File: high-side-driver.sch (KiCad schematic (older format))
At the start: 10 parts, among them Q1 CJ3139K, Q2 CJ3139K, Q3 CJ3139K, Q4 CJ3139K, Q5 CJ3139K, Q6 CJ3139K, Q7 CJ3139K, Q8 CJ3139K, U8 74HC595

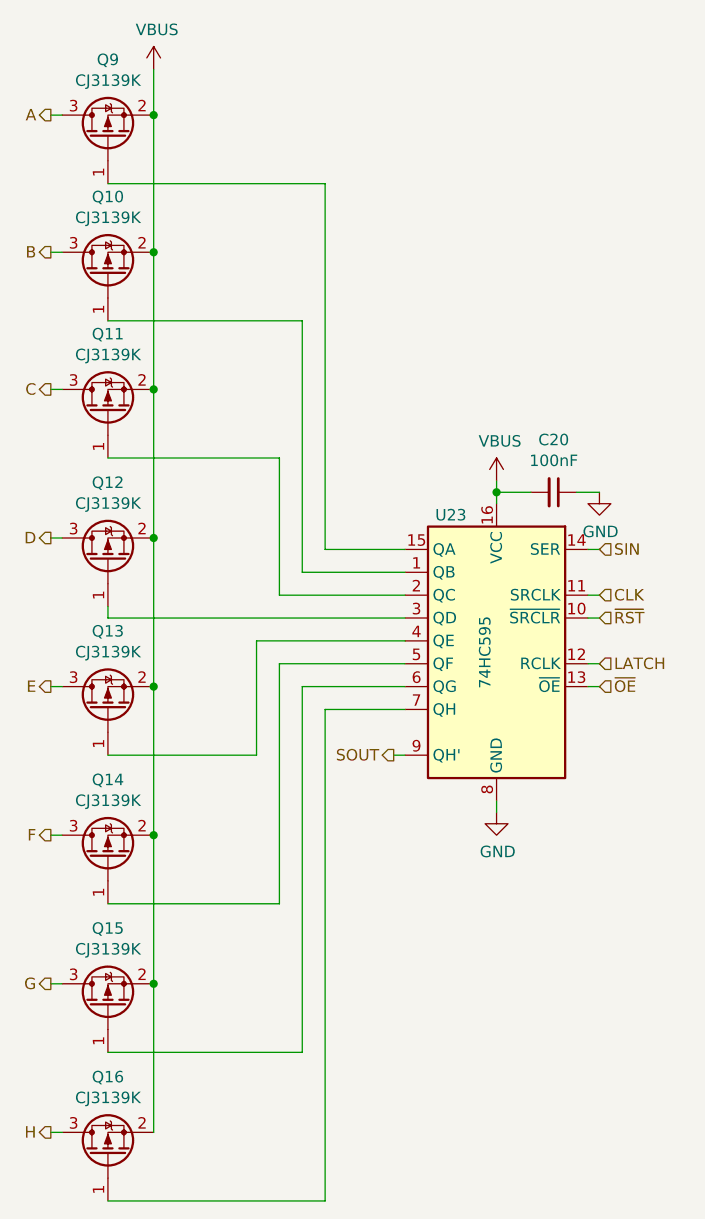
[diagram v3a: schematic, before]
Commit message: Add multiplexing MCU and USB
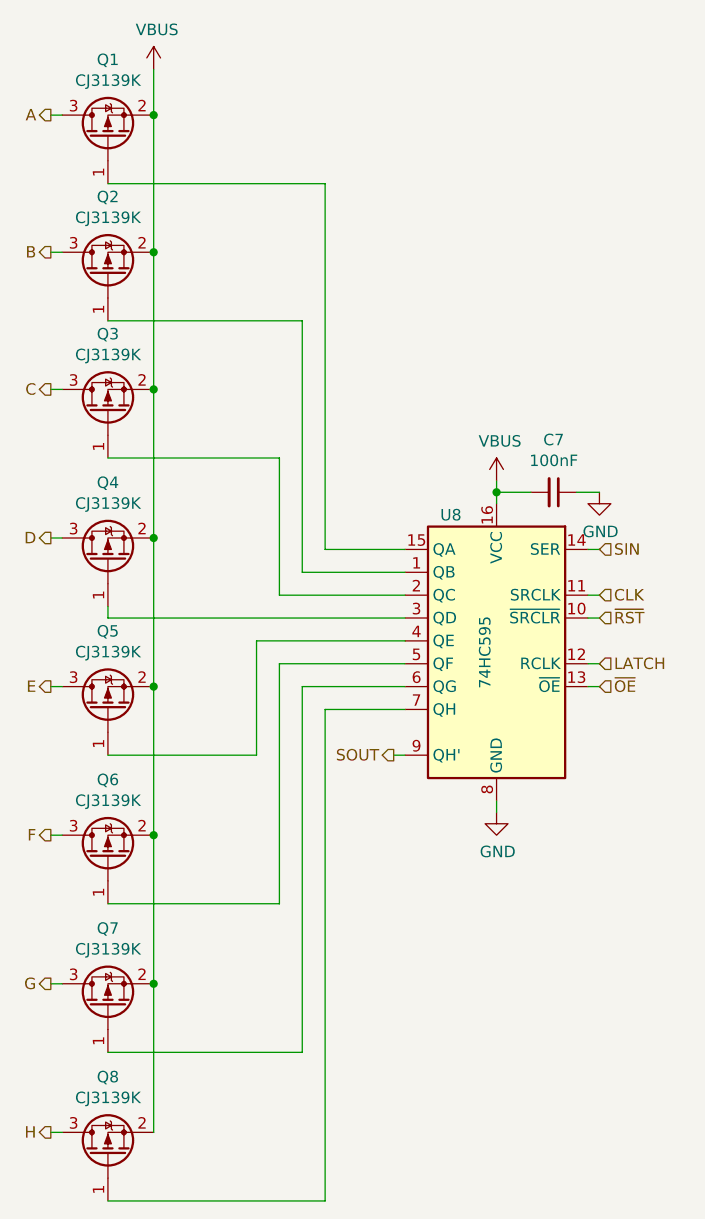
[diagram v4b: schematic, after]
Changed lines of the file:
@@
 $Descr A4 11693 8268
 encoding utf-8
-Sheet 24 25
+Sheet 9 25
 Title ""
 Date ""
@@
 AR Path="/61C25DCC/61C27AAF" Ref="#PWR0119"  Part="1"
 AR Path="/61C56D3D/61C27AAF" Ref="#PWR0159"  Part="1"
-F 0 "#PWR0159" H 5500 4100 50  0001 C CNN
+F 0 "#PWR0119" H 5500 4100 50  0001 C CNN
 F 1 "GND" H 5505 4177 50  0000 C CNN
 F 2 "" H 5500 4350 50  0001 C CNN
@@
 AR Path="/61C25DCC/61C27AC2" Ref="#PWR0120"  Part="1"
 AR Path="/61C56D3D/61C27AC2" Ref="#PWR0160"  Part="1"
-F 0 "#PWR0160" H 5950 2700 50  0001 C CNN
+F 0 "#PWR0120" H 5950 2700 50  0001 C CNN
 F 1 "GND" H 5955 2777 50  0000 C CNN
 F 2 "" H 5950 2950 50  0001 C CNN
@@
 AR Path="/61C25DCC/61C27AC9" Ref="C7"  Part="1"
 AR Path="/61C56D3D/61C27AC9" Ref="C20"  Part="1"
-F 0 "C20" V 5521 2950 50  0000 C CNN
+F 0 "C7" V 5521 2950 50  0000 C CNN
 F 1 "100nF" V 5612 2950 50  0000 C CNN
 F 2 "Capacitor_SMD:C_0402_1005Metric" H 5750 2950 50  0001 C CNN
@@
 AR Path="/61C25DCC/61C27AE4" Ref="#PWR0121"  Part="1"
 AR Path="/61C56D3D/61C27AE4" Ref="#PWR0161"  Part="1"
-F 0 "#PWR0161" H 5500 2750 50  0001 C CNN
+F 0 "#PWR0121" H 5500 2750 50  0001 C CNN
 F 1 "VBUS" H 5515 3073 50  0000 C CNN
 F 2 "" H 5500 2900 50  0001 C CNN
@@
 AR Path="/61C25DCC/61C27AFF" Ref="U8"  Part="1"
 AR Path="/61C56D3D/61C27AFF" Ref="U23"  Part="1"
-F 0 "U23" H 5700 4150 50  0000 C CNN
+F 0 "U8" H 5700 4150 50  0000 C CNN
 F 1 "74HC595" V 5550 3550 50  0000 C CNN
 F 2 "Package_Texas:X1QFN-16-2.5x2.5-EP-1.2" H 5500 3600 50  0001 C CNN
@@
 AR Path="/61C25DCC/61C2F27B" Ref="Q1"  Part="1"
 AR Path="/61C56D3D/61C2F27B" Ref="Q9"  Part="1"
-F 0 "Q9" V 4142 1400 50  0000 C CNN
+F 0 "Q1" V 4142 1400 50  0000 C CNN
 F 1 "CJ3139K" V 4051 1400 50  0000 C CNN
 F 2 "Package_TO_SOT_SMD:SOT-723" H 4000 1325 50  0001 L CIN
@@
 AR Path="/61C25DCC/61C3FEA0" Ref="#PWR0122"  Part="1"
 AR Path="/61C56D3D/61C3FEA0" Ref="#PWR0162"  Part="1"
-F 0 "#PWR0162" H 4000 950 50  0001 C CNN
+F 0 "#PWR0122" H 4000 950 50  0001 C CNN
 F 1 "VBUS" H 4015 1273 50  0000 C CNN
 F 2 "" H 4000 1100 50  0001 C CNN
@@
 AR Path="/61C25DCC/61C8820B" Ref="Q2"  Part="1"
 AR Path="/61C56D3D/61C8820B" Ref="Q10"  Part="1"
-F 0 "Q10" V 4142 2000 50  0000 C CNN
+F 0 "Q2" V 4142 2000 50  0000 C CNN
 F 1 "CJ3139K" V 4051 2000 50  0000 C CNN
 F 2 "Package_TO_SOT_SMD:SOT-723" H 4000 1925 50  0001 L CIN
@@
 AR Path="/61C25DCC/61C89C26" Ref="Q3"  Part="1"
 AR Path="/61C56D3D/61C89C26" Ref="Q11"  Part="1"
-F 0 "Q11" V 4142 2600 50  0000 C CNN
+F 0 "Q3" V 4142 2600 50  0000 C CNN
 F 1 "CJ3139K" V 4051 2600 50  0000 C CNN
 F 2 "Package_TO_SOT_SMD:SOT-723" H 4000 2525 50  0001 L CIN
@@
 AR Path="/61C25DCC/61C8B69B" Ref="Q4"  Part="1"
 AR Path="/61C56D3D/61C8B69B" Ref="Q12"  Part="1"
-F 0 "Q12" V 4142 3250 50  0000 C CNN
+F 0 "Q4" V 4142 3250 50  0000 C CNN
 F 1 "CJ3139K" V 4051 3250 50  0000 C CNN
 F 2 "Package_TO_SOT_SMD:SOT-723" H 4000 3175 50  0001 L CIN
@@
 AR Path="/61C25DCC/61C8D443" Ref="Q5"  Part="1"
 AR Path="/61C56D3D/61C8D443" Ref="Q13"  Part="1"
-F 0 "Q13" V 4142 3900 50  0000 C CNN
+F 0 "Q5" V 4142 3900 50  0000 C CNN
 F 1 "CJ3139K" V 4051 3900 50  0000 C CNN
 F 2 "Package_TO_SOT_SMD:SOT-723" H 4000 3825 50  0001 L CIN
@@
 AR Path="/61C25DCC/61C8EABF" Ref="Q6"  Part="1"
 AR Path="/61C56D3D/61C8EABF" Ref="Q14"  Part="1"
-F 0 "Q14" V 4142 4550 50  0000 C CNN
+F 0 "Q6" V 4142 4550 50  0000 C CNN
 F 1 "CJ3139K" V 4051 4550 50  0000 C CNN
 F 2 "Package_TO_SOT_SMD:SOT-723" H 4000 4475 50  0001 L CIN
@@
 AR Path="/61C25DCC/61C901AA" Ref="Q7"  Part="1"
 AR Path="/61C56D3D/61C901AA" Ref="Q15"  Part="1"
-F 0 "Q15" V 4142 5200 50  0000 C CNN
+F 0 "Q7" V 4142 5200 50  0000 C CNN
 F 1 "CJ3139K" V 4051 5200 50  0000 C CNN
 F 2 "Package_TO_SOT_SMD:SOT-723" H 4000 5125 50  0001 L CIN
@@
 AR Path="/61C25DCC/61C923B7" Ref="Q8"  Part="1"
 AR Path="/61C56D3D/61C923B7" Ref="Q16"  Part="1"
-F 0 "Q16" V 4142 5850 50  0000 C CNN
+F 0 "Q8" V 4142 5850 50  0000 C CNN
 F 1 "CJ3139K" V 4051 5850 50  0000 C CNN
 F 2 "Package_TO_SOT_SMD:SOT-723" H 4000 5775 50  0001 L CIN

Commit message: Add mounting pad for safety pin
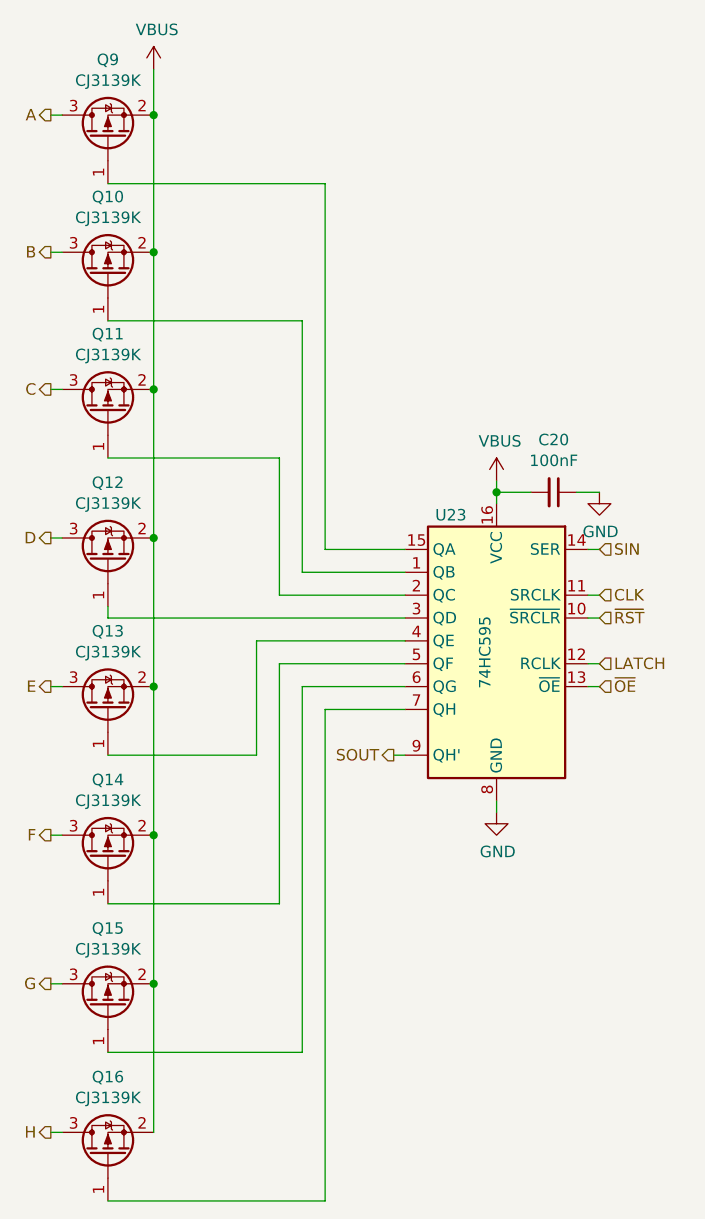
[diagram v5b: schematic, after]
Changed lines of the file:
@@
 AR Path="/61C25DCC/61C27AAF" Ref="#PWR0119"  Part="1"
 AR Path="/61C56D3D/61C27AAF" Ref="#PWR0159"  Part="1"
-F 0 "#PWR0119" H 5500 4100 50  0001 C CNN
+F 0 "#PWR0159" H 5500 4100 50  0001 C CNN
 F 1 "GND" H 5505 4177 50  0000 C CNN
 F 2 "" H 5500 4350 50  0001 C CNN
@@
 AR Path="/61C25DCC/61C27AC2" Ref="#PWR0120"  Part="1"
 AR Path="/61C56D3D/61C27AC2" Ref="#PWR0160"  Part="1"
-F 0 "#PWR0120" H 5950 2700 50  0001 C CNN
+F 0 "#PWR0160" H 5950 2700 50  0001 C CNN
 F 1 "GND" H 5955 2777 50  0000 C CNN
 F 2 "" H 5950 2950 50  0001 C CNN
@@
 AR Path="/61C25DCC/61C27AC9" Ref="C7"  Part="1"
 AR Path="/61C56D3D/61C27AC9" Ref="C20"  Part="1"
-F 0 "C7" V 5521 2950 50  0000 C CNN
+F 0 "C20" V 5521 2950 50  0000 C CNN
 F 1 "100nF" V 5612 2950 50  0000 C CNN
 F 2 "Capacitor_SMD:C_0402_1005Metric" H 5750 2950 50  0001 C CNN
@@
 AR Path="/61C25DCC/61C27AE4" Ref="#PWR0121"  Part="1"
 AR Path="/61C56D3D/61C27AE4" Ref="#PWR0161"  Part="1"
-F 0 "#PWR0121" H 5500 2750 50  0001 C CNN
+F 0 "#PWR0161" H 5500 2750 50  0001 C CNN
 F 1 "VBUS" H 5515 3073 50  0000 C CNN
 F 2 "" H 5500 2900 50  0001 C CNN
@@
 AR Path="/61C25DCC/61C27AFF" Ref="U8"  Part="1"
 AR Path="/61C56D3D/61C27AFF" Ref="U23"  Part="1"
-F 0 "U8" H 5700 4150 50  0000 C CNN
+F 0 "U23" H 5700 4150 50  0000 C CNN
 F 1 "74HC595" V 5550 3550 50  0000 C CNN
 F 2 "Package_Texas:X1QFN-16-2.5x2.5-EP-1.2" H 5500 3600 50  0001 C CNN
@@
 AR Path="/61C25DCC/61C2F27B" Ref="Q1"  Part="1"
 AR Path="/61C56D3D/61C2F27B" Ref="Q9"  Part="1"
-F 0 "Q1" V 4142 1400 50  0000 C CNN
+F 0 "Q9" V 4142 1400 50  0000 C CNN
 F 1 "CJ3139K" V 4051 1400 50  0000 C CNN
 F 2 "Package_TO_SOT_SMD:SOT-723" H 4000 1325 50  0001 L CIN
@@
 AR Path="/61C25DCC/61C3FEA0" Ref="#PWR0122"  Part="1"
 AR Path="/61C56D3D/61C3FEA0" Ref="#PWR0162"  Part="1"
-F 0 "#PWR0122" H 4000 950 50  0001 C CNN
+F 0 "#PWR0162" H 4000 950 50  0001 C CNN
 F 1 "VBUS" H 4015 1273 50  0000 C CNN
 F 2 "" H 4000 1100 50  0001 C CNN
@@
 AR Path="/61C25DCC/61C8820B" Ref="Q2"  Part="1"
 AR Path="/61C56D3D/61C8820B" Ref="Q10"  Part="1"
-F 0 "Q2" V 4142 2000 50  0000 C CNN
+F 0 "Q10" V 4142 2000 50  0000 C CNN
 F 1 "CJ3139K" V 4051 2000 50  0000 C CNN
 F 2 "Package_TO_SOT_SMD:SOT-723" H 4000 1925 50  0001 L CIN
@@
 AR Path="/61C25DCC/61C89C26" Ref="Q3"  Part="1"
 AR Path="/61C56D3D/61C89C26" Ref="Q11"  Part="1"
-F 0 "Q3" V 4142 2600 50  0000 C CNN
+F 0 "Q11" V 4142 2600 50  0000 C CNN
 F 1 "CJ3139K" V 4051 2600 50  0000 C CNN
 F 2 "Package_TO_SOT_SMD:SOT-723" H 4000 2525 50  0001 L CIN
@@
 AR Path="/61C25DCC/61C8B69B" Ref="Q4"  Part="1"
 AR Path="/61C56D3D/61C8B69B" Ref="Q12"  Part="1"
-F 0 "Q4" V 4142 3250 50  0000 C CNN
+F 0 "Q12" V 4142 3250 50  0000 C CNN
 F 1 "CJ3139K" V 4051 3250 50  0000 C CNN
 F 2 "Package_TO_SOT_SMD:SOT-723" H 4000 3175 50  0001 L CIN
@@
 AR Path="/61C25DCC/61C8D443" Ref="Q5"  Part="1"
 AR Path="/61C56D3D/61C8D443" Ref="Q13"  Part="1"
-F 0 "Q5" V 4142 3900 50  0000 C CNN
+F 0 "Q13" V 4142 3900 50  0000 C CNN
 F 1 "CJ3139K" V 4051 3900 50  0000 C CNN
 F 2 "Package_TO_SOT_SMD:SOT-723" H 4000 3825 50  0001 L CIN
@@
 AR Path="/61C25DCC/61C8EABF" Ref="Q6"  Part="1"
 AR Path="/61C56D3D/61C8EABF" Ref="Q14"  Part="1"
-F 0 "Q6" V 4142 4550 50  0000 C CNN
+F 0 "Q14" V 4142 4550 50  0000 C CNN
 F 1 "CJ3139K" V 4051 4550 50  0000 C CNN
 F 2 "Package_TO_SOT_SMD:SOT-723" H 4000 4475 50  0001 L CIN
@@
 AR Path="/61C25DCC/61C901AA" Ref="Q7"  Part="1"
 AR Path="/61C56D3D/61C901AA" Ref="Q15"  Part="1"
-F 0 "Q7" V 4142 5200 50  0000 C CNN
+F 0 "Q15" V 4142 5200 50  0000 C CNN
 F 1 "CJ3139K" V 4051 5200 50  0000 C CNN
 F 2 "Package_TO_SOT_SMD:SOT-723" H 4000 5125 50  0001 L CIN
@@
 AR Path="/61C25DCC/61C923B7" Ref="Q8"  Part="1"
 AR Path="/61C56D3D/61C923B7" Ref="Q16"  Part="1"
-F 0 "Q8" V 4142 5850 50  0000 C CNN
+F 0 "Q16" V 4142 5850 50  0000 C CNN
 F 1 "CJ3139K" V 4051 5850 50  0000 C CNN
 F 2 "Package_TO_SOT_SMD:SOT-723" H 4000 5775 50  0001 L CIN

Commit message: Use better ESP32 Pico D4 footprint
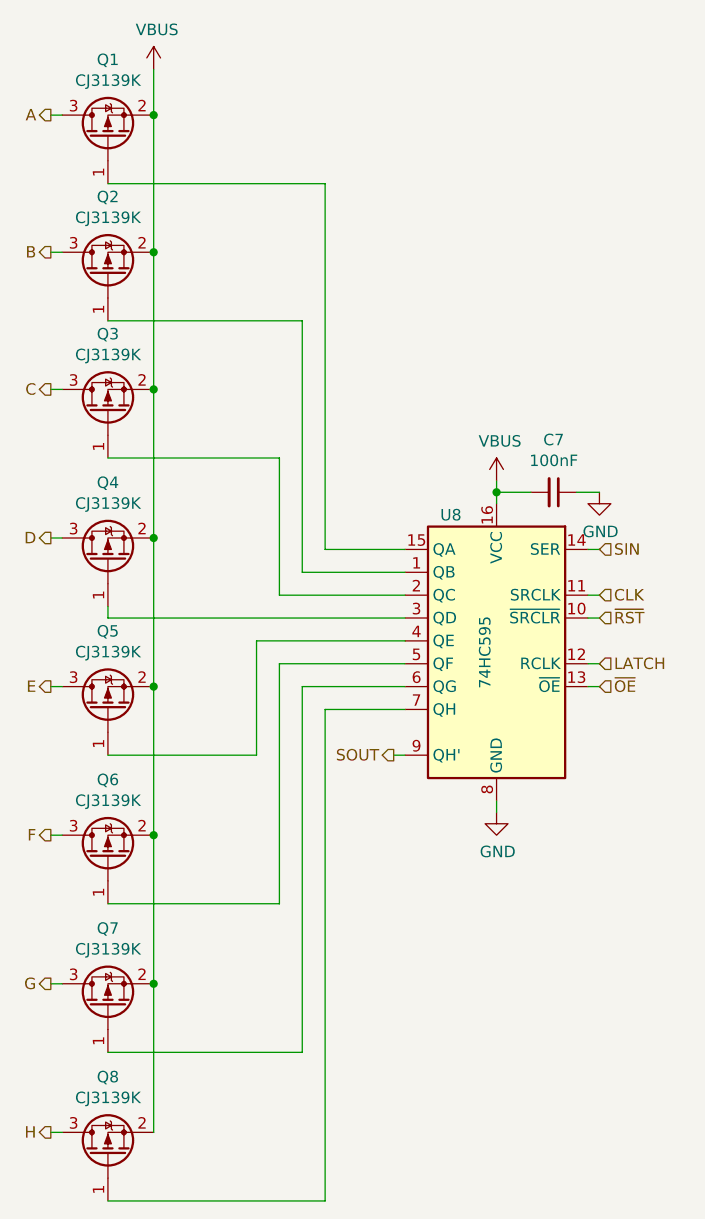
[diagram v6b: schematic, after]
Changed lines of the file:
@@
 AR Path="/61C25DCC/61C27AC9" Ref="C7"  Part="1"
 AR Path="/61C56D3D/61C27AC9" Ref="C20"  Part="1"
-F 0 "C20" V 5521 2950 50  0000 C CNN
+F 0 "C7" V 5521 2950 50  0000 C CNN
 F 1 "100nF" V 5612 2950 50  0000 C CNN
 F 2 "Capacitor_SMD:C_0402_1005Metric" H 5750 2950 50  0001 C CNN
@@
 AR Path="/61C25DCC/61C27AFF" Ref="U8"  Part="1"
 AR Path="/61C56D3D/61C27AFF" Ref="U23"  Part="1"
-F 0 "U23" H 5700 4150 50  0000 C CNN
+F 0 "U8" H 5700 4150 50  0000 C CNN
 F 1 "74HC595" V 5550 3550 50  0000 C CNN
 F 2 "Package_Texas:X1QFN-16-2.5x2.5-EP-1.2" H 5500 3600 50  0001 C CNN
@@
 AR Path="/61C25DCC/61C2F27B" Ref="Q1"  Part="1"
 AR Path="/61C56D3D/61C2F27B" Ref="Q9"  Part="1"
-F 0 "Q9" V 4142 1400 50  0000 C CNN
+F 0 "Q1" V 4142 1400 50  0000 C CNN
 F 1 "CJ3139K" V 4051 1400 50  0000 C CNN
 F 2 "Package_TO_SOT_SMD:SOT-723" H 4000 1325 50  0001 L CIN
@@
 AR Path="/61C25DCC/61C8820B" Ref="Q2"  Part="1"
 AR Path="/61C56D3D/61C8820B" Ref="Q10"  Part="1"
-F 0 "Q10" V 4142 2000 50  0000 C CNN
+F 0 "Q2" V 4142 2000 50  0000 C CNN
 F 1 "CJ3139K" V 4051 2000 50  0000 C CNN
 F 2 "Package_TO_SOT_SMD:SOT-723" H 4000 1925 50  0001 L CIN
@@
 AR Path="/61C25DCC/61C89C26" Ref="Q3"  Part="1"
 AR Path="/61C56D3D/61C89C26" Ref="Q11"  Part="1"
-F 0 "Q11" V 4142 2600 50  0000 C CNN
+F 0 "Q3" V 4142 2600 50  0000 C CNN
 F 1 "CJ3139K" V 4051 2600 50  0000 C CNN
 F 2 "Package_TO_SOT_SMD:SOT-723" H 4000 2525 50  0001 L CIN
@@
 AR Path="/61C25DCC/61C8B69B" Ref="Q4"  Part="1"
 AR Path="/61C56D3D/61C8B69B" Ref="Q12"  Part="1"
-F 0 "Q12" V 4142 3250 50  0000 C CNN
+F 0 "Q4" V 4142 3250 50  0000 C CNN
 F 1 "CJ3139K" V 4051 3250 50  0000 C CNN
 F 2 "Package_TO_SOT_SMD:SOT-723" H 4000 3175 50  0001 L CIN
@@
 AR Path="/61C25DCC/61C8D443" Ref="Q5"  Part="1"
 AR Path="/61C56D3D/61C8D443" Ref="Q13"  Part="1"
-F 0 "Q13" V 4142 3900 50  0000 C CNN
+F 0 "Q5" V 4142 3900 50  0000 C CNN
 F 1 "CJ3139K" V 4051 3900 50  0000 C CNN
 F 2 "Package_TO_SOT_SMD:SOT-723" H 4000 3825 50  0001 L CIN
@@
 AR Path="/61C25DCC/61C8EABF" Ref="Q6"  Part="1"
 AR Path="/61C56D3D/61C8EABF" Ref="Q14"  Part="1"
-F 0 "Q14" V 4142 4550 50  0000 C CNN
+F 0 "Q6" V 4142 4550 50  0000 C CNN
 F 1 "CJ3139K" V 4051 4550 50  0000 C CNN
 F 2 "Package_TO_SOT_SMD:SOT-723" H 4000 4475 50  0001 L CIN
@@
 AR Path="/61C25DCC/61C901AA" Ref="Q7"  Part="1"
 AR Path="/61C56D3D/61C901AA" Ref="Q15"  Part="1"
-F 0 "Q15" V 4142 5200 50  0000 C CNN
+F 0 "Q7" V 4142 5200 50  0000 C CNN
 F 1 "CJ3139K" V 4051 5200 50  0000 C CNN
 F 2 "Package_TO_SOT_SMD:SOT-723" H 4000 5125 50  0001 L CIN
@@
 AR Path="/61C25DCC/61C923B7" Ref="Q8"  Part="1"
 AR Path="/61C56D3D/61C923B7" Ref="Q16"  Part="1"
-F 0 "Q16" V 4142 5850 50  0000 C CNN
+F 0 "Q8" V 4142 5850 50  0000 C CNN
 F 1 "CJ3139K" V 4051 5850 50  0000 C CNN
 F 2 "Package_TO_SOT_SMD:SOT-723" H 4000 5775 50  0001 L CIN

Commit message: Add additional VBUS bulk capacitance
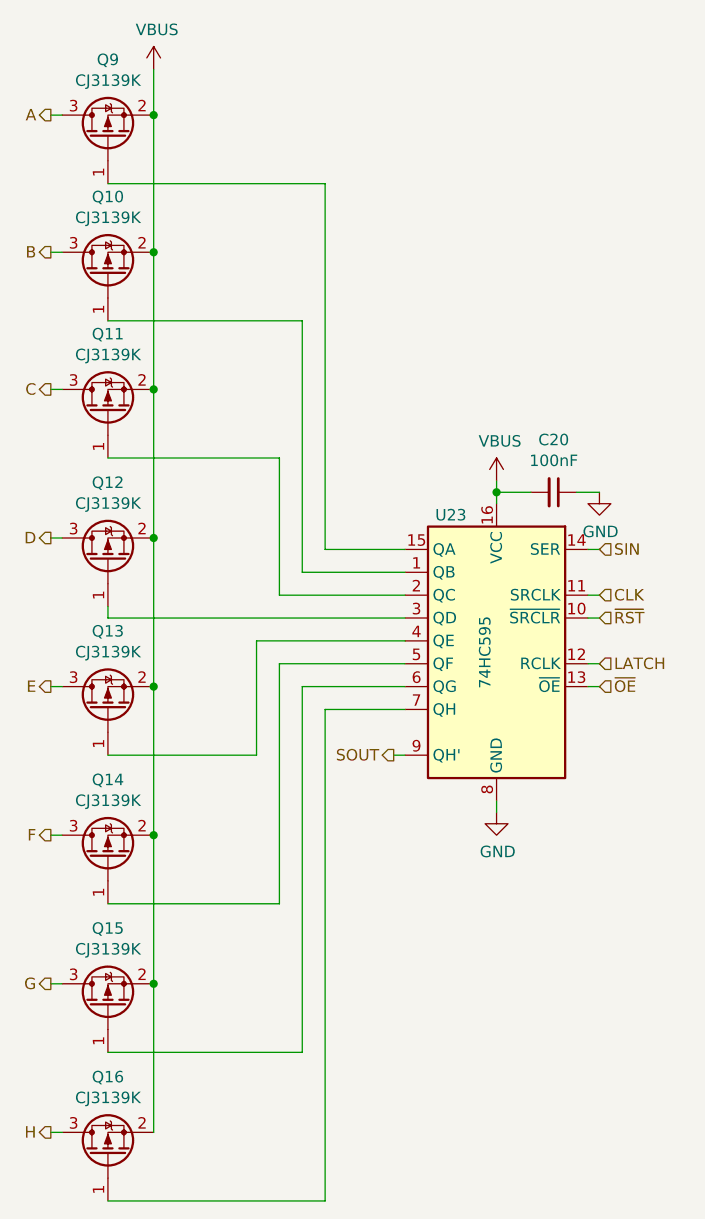
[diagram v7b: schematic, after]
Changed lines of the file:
@@
 AR Path="/61C25DCC/61C27AC9" Ref="C7"  Part="1"
 AR Path="/61C56D3D/61C27AC9" Ref="C20"  Part="1"
-F 0 "C7" V 5521 2950 50  0000 C CNN
+F 0 "C20" V 5521 2950 50  0000 C CNN
 F 1 "100nF" V 5612 2950 50  0000 C CNN
 F 2 "Capacitor_SMD:C_0402_1005Metric" H 5750 2950 50  0001 C CNN
@@
 AR Path="/61C25DCC/61C27AFF" Ref="U8"  Part="1"
 AR Path="/61C56D3D/61C27AFF" Ref="U23"  Part="1"
-F 0 "U8" H 5700 4150 50  0000 C CNN
+F 0 "U23" H 5700 4150 50  0000 C CNN
 F 1 "74HC595" V 5550 3550 50  0000 C CNN
 F 2 "Package_Texas:X1QFN-16-2.5x2.5-EP-1.2" H 5500 3600 50  0001 C CNN
@@
 AR Path="/61C25DCC/61C2F27B" Ref="Q1"  Part="1"
 AR Path="/61C56D3D/61C2F27B" Ref="Q9"  Part="1"
-F 0 "Q1" V 4142 1400 50  0000 C CNN
+F 0 "Q9" V 4142 1400 50  0000 C CNN
 F 1 "CJ3139K" V 4051 1400 50  0000 C CNN
 F 2 "Package_TO_SOT_SMD:SOT-723" H 4000 1325 50  0001 L CIN
@@
 AR Path="/61C25DCC/61C8820B" Ref="Q2"  Part="1"
 AR Path="/61C56D3D/61C8820B" Ref="Q10"  Part="1"
-F 0 "Q2" V 4142 2000 50  0000 C CNN
+F 0 "Q10" V 4142 2000 50  0000 C CNN
 F 1 "CJ3139K" V 4051 2000 50  0000 C CNN
 F 2 "Package_TO_SOT_SMD:SOT-723" H 4000 1925 50  0001 L CIN
@@
 AR Path="/61C25DCC/61C89C26" Ref="Q3"  Part="1"
 AR Path="/61C56D3D/61C89C26" Ref="Q11"  Part="1"
-F 0 "Q3" V 4142 2600 50  0000 C CNN
+F 0 "Q11" V 4142 2600 50  0000 C CNN
 F 1 "CJ3139K" V 4051 2600 50  0000 C CNN
 F 2 "Package_TO_SOT_SMD:SOT-723" H 4000 2525 50  0001 L CIN
@@
 AR Path="/61C25DCC/61C8B69B" Ref="Q4"  Part="1"
 AR Path="/61C56D3D/61C8B69B" Ref="Q12"  Part="1"
-F 0 "Q4" V 4142 3250 50  0000 C CNN
+F 0 "Q12" V 4142 3250 50  0000 C CNN
 F 1 "CJ3139K" V 4051 3250 50  0000 C CNN
 F 2 "Package_TO_SOT_SMD:SOT-723" H 4000 3175 50  0001 L CIN
@@
 AR Path="/61C25DCC/61C8D443" Ref="Q5"  Part="1"
 AR Path="/61C56D3D/61C8D443" Ref="Q13"  Part="1"
-F 0 "Q5" V 4142 3900 50  0000 C CNN
+F 0 "Q13" V 4142 3900 50  0000 C CNN
 F 1 "CJ3139K" V 4051 3900 50  0000 C CNN
 F 2 "Package_TO_SOT_SMD:SOT-723" H 4000 3825 50  0001 L CIN
@@
 AR Path="/61C25DCC/61C8EABF" Ref="Q6"  Part="1"
 AR Path="/61C56D3D/61C8EABF" Ref="Q14"  Part="1"
-F 0 "Q6" V 4142 4550 50  0000 C CNN
+F 0 "Q14" V 4142 4550 50  0000 C CNN
 F 1 "CJ3139K" V 4051 4550 50  0000 C CNN
 F 2 "Package_TO_SOT_SMD:SOT-723" H 4000 4475 50  0001 L CIN
@@
 AR Path="/61C25DCC/61C901AA" Ref="Q7"  Part="1"
 AR Path="/61C56D3D/61C901AA" Ref="Q15"  Part="1"
-F 0 "Q7" V 4142 5200 50  0000 C CNN
+F 0 "Q15" V 4142 5200 50  0000 C CNN
 F 1 "CJ3139K" V 4051 5200 50  0000 C CNN
 F 2 "Package_TO_SOT_SMD:SOT-723" H 4000 5125 50  0001 L CIN
@@
 AR Path="/61C25DCC/61C923B7" Ref="Q8"  Part="1"
 AR Path="/61C56D3D/61C923B7" Ref="Q16"  Part="1"
-F 0 "Q8" V 4142 5850 50  0000 C CNN
+F 0 "Q16" V 4142 5850 50  0000 C CNN
 F 1 "CJ3139K" V 4051 5850 50  0000 C CNN
 F 2 "Package_TO_SOT_SMD:SOT-723" H 4000 5775 50  0001 L CIN
